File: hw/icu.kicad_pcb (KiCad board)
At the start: 2 copper layers, 60 x 90 mm, 107 parts, among them J1001 ARM_JTAG_SWD_HEADER_10_PINSMD, J101 AMPSEAL_8_POS_VERT_BLACK_SEAL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, J102 AMPSEAL_23_POS_VERT_GRAY_SEAL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, U1001 MCP2551_SOIC8, U1002 LPC1549JBD64, U301 VND5050AJTR-E, U401 VND5050AJTR-E, U501 VND5050AJTR-E, U601 VND5050AJTR-E, U701 VND5050AJTR-E, U801 VND5050AJTR-E, U901 VND5050AJTR-E, X1001 XTAL_7A-12.000MAAJ-T

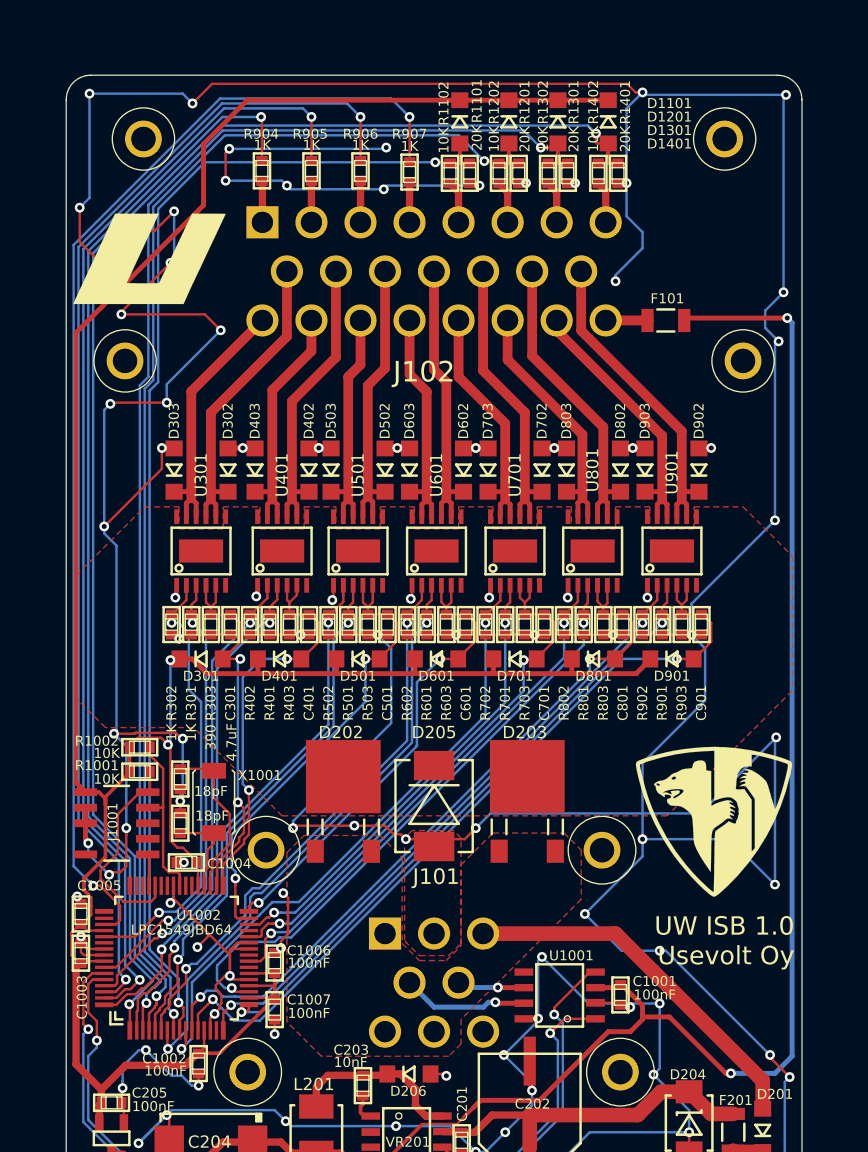
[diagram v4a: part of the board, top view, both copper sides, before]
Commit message: analog inputs replaced with digital inputs
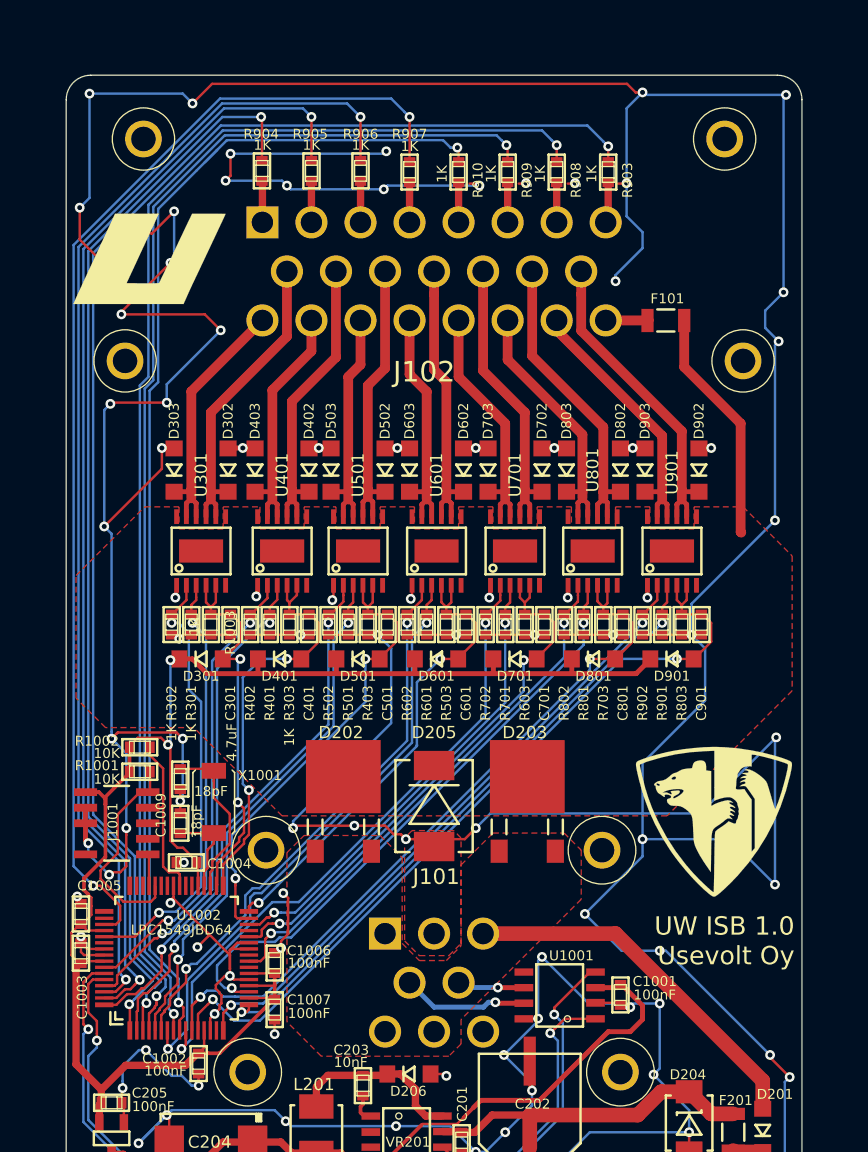
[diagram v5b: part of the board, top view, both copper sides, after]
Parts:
- removed D1101, D1201, D1301, D1401: DIODE_RS07J-GS18, usevolt:DO219AB
- removed R1101, R1201, R1301, R1401: 10K, yageo:0603
- removed R1102, R1202, R1302, R1402: 20K, yageo:0603
- removed eC1009: 18pF, kemet:0603
- added C1009: 18pF, kemet:0603, F.Cu at (147.3, 110.0)
- added R1003: 1K, yageo:0603, F.Cu at (149.8, 93.8)
- added R908: 1K, yageo:0603, F.Cu at (178.0, 56.9)
- added R909: 1K, yageo:0603, F.Cu at (174.0, 56.9)
- added R910: 1K, yageo:0603, F.Cu at (170.0, 56.9)
- R303, R403, R503, R603, R703, R803, R903: value 390 -> 1K
- moved R903 37.4 mm to (182.2, 56.9)
- moved R403 6.40 mm to (162.6, 93.8)
- moved R503 6.40 mm to (169.0, 93.8)
- moved R603 6.40 mm to (175.4, 93.8)
- moved R703 6.40 mm to (181.8, 93.8)
- moved R303 6.40 mm to (156.2, 93.8)
- moved R803 6.40 mm to (188.2, 93.8)
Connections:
- F101 pad P$1: +5V -> VDD
- J102 pad 5: /Sheet5A7E031D/VIN -> /lpc1549/DIN5
- J102 pad 6: /Sheet5A7E2A6D/VIN -> /lpc1549/DIN6
- J102 pad 7: /Sheet5A7E34B9/VIN -> /lpc1549/DIN7
- J102 pad 8: /Sheet5A8C5347/VIN -> /lpc1549/DIN8
- R303 pad 1: /lpc1549/OUT1_SENSE -> /lpc1549/OUT2_SENSE
- R403 pad 1: /lpc1549/OUT2_SENSE -> /lpc1549/OUT3_SENSE
- R503 pad 1: /lpc1549/OUT3_SENSE -> /lpc1549/OUT4_SENSE
- R603 pad 1: /lpc1549/OUT4_SENSE -> /lpc1549/OUT5_SENSE
- R703 pad 1: /lpc1549/OUT5_SENSE -> /lpc1549/OUT6_SENSE
- R803 pad 1: /lpc1549/OUT6_SENSE -> /lpc1549/OUT7_SENSE
- R903 pad 1: /lpc1549/OUT7_SENSE -> Net-(R903-Pad1)
- R903 pad 2: GND -> /lpc1549/DIN8
- U1002 pad P$3: /lpc1549/AIN4 -> Net-(R903-Pad1)
- U1002 pad P$4: /lpc1549/AIN3 -> Net-(R908-Pad1)
- U1002 pad P$8: /lpc1549/AIN2 -> Net-(R909-Pad1)
- U1002 pad P$9: /lpc1549/AIN1 -> Net-(R910-Pad1)
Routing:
- net /lpc1549/AIN4: track 117.1 -> 0.00 mm, vias 2 -> 0
- net Net-(R903-Pad1): track 0.00 -> 114.6 mm, vias 0 -> 2
- net /lpc1549/AIN3: track 108.9 -> 0.00 mm, vias 2 -> 0
- net Net-(R908-Pad1): track 0.00 -> 106.7 mm, vias 0 -> 2
- net /lpc1549/AIN2: track 103.3 -> 0.00 mm, vias 2 -> 0
- net Net-(R909-Pad1): track 0.00 -> 101.5 mm, vias 0 -> 2
- net Net-(R910-Pad1): track 0.00 -> 98.1 mm, vias 0 -> 2
- net /lpc1549/AIN1: track 97.2 -> 0.00 mm, vias 2 -> 0
- net +3V3: track 230.6 -> 138.6 mm
- net +5V: track 139.3 -> 55.7 mm, vias 2 -> 0
- net VDD: track 0.00 -> 19.2 mm
- net /Sheet5A8C5347/VIN: track 3.69 -> 0.00 mm
- net /lpc1549/DIN8: track 0.00 -> 3.63 mm
- net /Sheet5A7E34B9/VIN: track 3.45 -> 0.00 mm
- net /Sheet5A7E2A6D/VIN: track 3.45 -> 0.00 mm
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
